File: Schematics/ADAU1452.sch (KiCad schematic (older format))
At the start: 97 parts, among them CN201 COAX, P201 CONN_2x1, P203 CONN_6X2, P204 CONN_6x1, SW202 SWITCH, U201 ADAU1452WBCPZ, U202 ADM13307-5ARZ, U203 25AA1024, X201 24M576

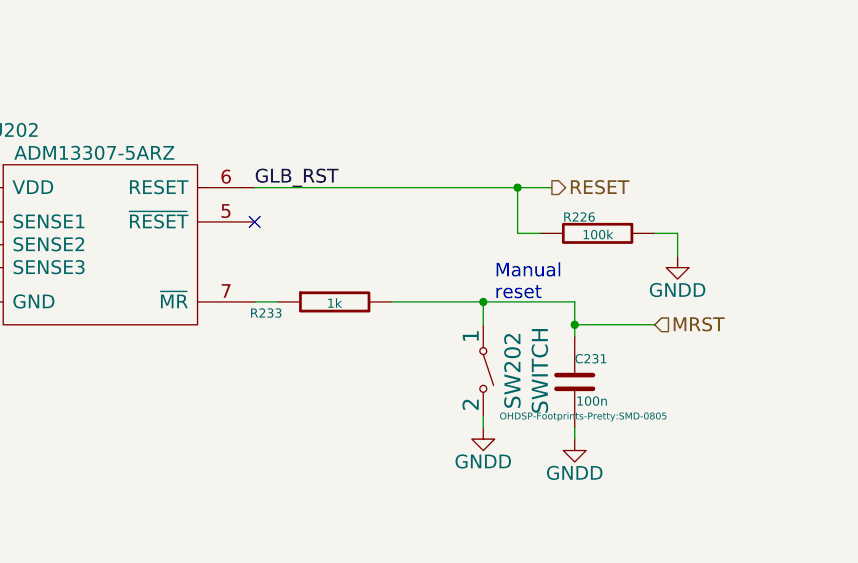
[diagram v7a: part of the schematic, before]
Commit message: PCB work, ADAU reset changes
Added caps to reset lines
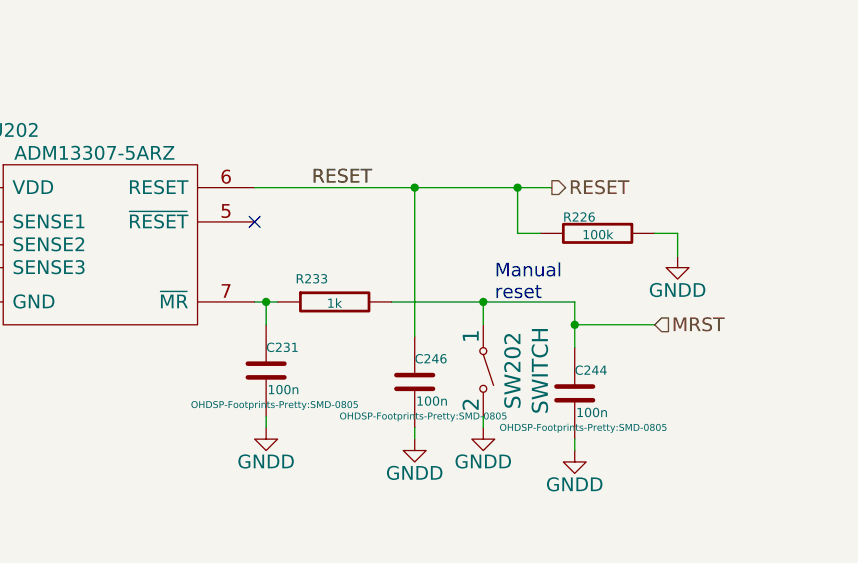
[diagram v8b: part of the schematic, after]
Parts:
- added C244, C246: 100n, OHDSP-Footprints-Pretty:SMD-0805, symbol C
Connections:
- net labels removed: GLB_RST
- wire segments 323 -> 327
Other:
- moved on the sheet: C231
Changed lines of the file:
@@
 	0    1    1    0
 $EndComp
-Text Label 8350 9500 0    60   ~ 0
-GLB_RST
 $Comp
 L R R226
@@
 L C C231
 U 1 1 54EA1193
-P 9750 10350
-F 0 "C231" H 9750 10450 40  0000 L CNN
-F 1 "100n" H 9756 10265 40  0000 L CNN
-F 2 "OHDSP-Footprints-Pretty:SMD-0805" H 9788 10200 30  0000 C CNN
-F 3 "~" H 9750 10350 60  0000 C CNN
-	1    9750 10350
+P 8400 10300
+F 0 "C231" H 8400 10400 40  0000 L CNN
+F 1 "100n" H 8406 10215 40  0000 L CNN
+F 2 "OHDSP-Footprints-Pretty:SMD-0805" H 8438 10150 30  0000 C CNN
+F 3 "~" H 8400 10300 60  0000 C CNN
+	1    8400 10300
 	1    0    0    -1
 $EndComp
@@
 L GNDD #PWR029
 U 1 1 54EA141D
-P 9750 10600
-F 0 "#PWR029" H 9750 10350 60  0001 C CNN
-F 1 "GNDD" H 9750 10450 60  0000 C CNN
-F 2 "" H 9750 10600 60  0000 C CNN
-F 3 "" H 9750 10600 60  0000 C CNN
-	1    9750 10600
+P 8400 10550
+F 0 "#PWR029" H 8400 10300 60  0001 C CNN
+F 1 "GNDD" H 8400 10400 60  0000 C CNN
+F 2 "" H 8400 10550 60  0000 C CNN
+F 3 "" H 8400 10550 60  0000 C CNN
+	1    8400 10550
 	-1   0    0    -1
 $EndComp
@@
 U 1 1 54F0DD27
 P 8700 10000
-F 0 "R233" V 8750 10300 40  0000 C CNN
+F 0 "R233" V 8600 10100 40  0000 C CNN
 F 1 "1k" V 8707 10001 40  0000 C CNN
 F 2 "OHDSP-Footprints-Pretty:SMD-0805" V 8630 10000 30  0001 C CNN
@@
 	9350 10550 9350 10500
 Wire Wire Line
-	9750 10600 9750 10550
-Wire Wire Line
-	9750 10000 9750 10150
+	8400 10550 8400 10500
+Wire Wire Line
+	9750 10000 9750 10200
 Connection ~ 9350 10000
 Wire Wire Line
@@
 	10200 9700 10200 9800
 Wire Wire Line
-	8450 10000 8350 10000
+	8350 10000 8450 10000
 Wire Wire Line
 	8950 10000 9750 10000
@@
 Wire Wire Line
 	14650 5550 14500 5550
+Wire Wire Line
+	8400 10100 8400 10000
+Connection ~ 8400 10000
+$Comp
+L C C244
+U 1 1 54FF35A4
+P 9750 10400
+F 0 "C244" H 9750 10500 40  0000 L CNN
+F 1 "100n" H 9756 10315 40  0000 L CNN
+F 2 "OHDSP-Footprints-Pretty:SMD-0805" H 9788 10250 30  0000 C CNN
+F 3 "~" H 9750 10400 60  0000 C CNN
+	1    9750 10400
+	1    0    0    -1
+$EndComp
+$Comp
+L GNDD #PWR040
+U 1 1 54FF363C
+P 9750 10650
+F 0 "#PWR040" H 9750 10400 60  0001 C CNN
+F 1 "GNDD" H 9750 10500 60  0000 C CNN
+F 2 "" H 9750 10650 60  0000 C CNN
+F 3 "" H 9750 10650 60  0000 C CNN
+	1    9750 10650
+	-1   0    0    -1
+$EndComp
+Wire Wire Line
+	9750 10650 9750 10600
+Text Label 8600 9500 0    60   ~ 0
+RESET
+$Comp
+L C C246
+U 1 1 54FF7B65
+P 9050 10350
+F 0 "C246" H 9050 10450 40  0000 L CNN
+F 1 "100n" H 9056 10265 40  0000 L CNN
+F 2 "OHDSP-Footprints-Pretty:SMD-0805" H 9088 10200 30  0000 C CNN
+F 3 "~" H 9050 10350 60  0000 C CNN
+	1    9050 10350
+	1    0    0    -1
+$EndComp
+$Comp
+L GNDD #PWR041
+U 1 1 54FF7C76
+P 9050 10600
+F 0 "#PWR041" H 9050 10350 60  0001 C CNN
+F 1 "GNDD" H 9050 10450 60  0000 C CNN
+F 2 "" H 9050 10600 60  0000 C CNN
+F 3 "" H 9050 10600 60  0000 C CNN
+	1    9050 10600
+	-1   0    0    -1
+$EndComp
+Wire Wire Line
+	9050 10600 9050 10550
+Wire Wire Line
+	9050 10150 9050 9500
+Connection ~ 9050 9500
 $EndSCHEMATC
